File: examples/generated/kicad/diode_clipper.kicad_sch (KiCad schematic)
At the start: 3 parts

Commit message: Attempt to fix more terminal issues.
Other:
- moved on the sheet: D1
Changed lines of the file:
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@@
+    )
+  )
+  (symbol (lib_id "GND") (at 56.00 105.62 0) (unit 1)
+    (in_bom yes) (on_board yes)
+    (property "Reference" "#PWR0001" (at 56.0 101.81 0)
+      (effects (font (size 1.27 1.27)) hide)
+    )
+    (property "Value" "GND" (at 56.0 109.43 0)
+      (effects (font (size 1.27 1.27)))
+    )
+    (property "Footprint" "" (at 0 0 0)
+      (effects (font (size 1.27 1.27)) hide)
+    )
+    (property "Datasheet" "" (at 0 0 0)
+      (effects (font (size 1.27 1.27)) hide)
     )
   )
@@
     )
   )
-  (symbol (lib_id "DIODE") (at 90.00 112.00 0) (unit 1)
+  (symbol (lib_id "DIODE") (at 96.35 95.08 270) (unit 1)
     (in_bom yes) (on_board yes)
-    (property "Reference" "D1" (at 90.0 104.0 0)
+    (property "Reference" "D1" (at 96.35 87.08 0)
       (effects (font (size 1.27 1.27)))
     )
-    (property "Value" "D4148" (at 90.0 120.0 0)
+    (property "Value" "D4148" (at 96.35 103.08 0)
       (effects (font (size 1.27 1.27)))
     )
@@
     )
   )
-  (symbol (lib_id "GND") (at 56.00 105.62 0) (unit 1)
+  (symbol (lib_id "GND") (at 96.35 112.16 0) (unit 1)
     (in_bom yes) (on_board yes)
-    (property "Reference" "#PWR0001" (at 56.0 101.81 0)
+    (property "Reference" "#PWR0002" (at 96.35 108.35 0)
       (effects (font (size 1.27 1.27)) hide)
     )
-    (property "Value" "GND" (at 56.0 109.43 0)
+    (property "Value" "GND" (at 96.35 115.97 0)
       (effects (font (size 1.27 1.27)))
     )
@@
     )
   )
-  (symbol (lib_id "GND") (at 105.08 118.00 0) (unit 1)
-    (in_bom yes) (on_board yes)
-    (property "Reference" "#PWR0002" (at 105.08 114.19 0)
-      (effects (font (size 1.27 1.27)) hide)
-    )
-    (property "Value" "GND" (at 105.08 121.81 0)
-      (effects (font (size 1.27 1.27)))
-    )
-    (property "Footprint" "" (at 0 0 0)
-      (effects (font (size 1.27 1.27)) hide)
-    )
-    (property "Datasheet" "" (at 0 0 0)
-      (effects (font (size 1.27 1.27)) hide)
-    )
+  (wire (pts (xy 96.35 100.16) (xy 96.35 112.16))
+    (stroke (width 0) (type solid) (color 0 0 0 0))
   )
   (wire (pts (xy 56.00 93.62) (xy 56.00 105.62))
-    (stroke (width 0) (type solid) (color 0 0 0 0))
-  )
-  (wire (pts (xy 95.08 112.00) (xy 105.08 112.00))
-    (stroke (width 0) (type solid) (color 0 0 0 0))
-  )
-  (wire (pts (xy 105.08 112.00) (xy 105.08 118.00))
     (stroke (width 0) (type solid) (color 0 0 0 0))
   )
@@
     (stroke (width 0) (type solid) (color 0 0 0 0))
   )
-  (wire (pts (xy 96.35 78.00) (xy 98.50 78.00))
-    (stroke (width 0) (type solid) (color 0 0 0 0))
-  )
-  (wire (pts (xy 98.50 78.00) (xy 98.50 105.00))
-    (stroke (width 0) (type solid) (color 0 0 0 0))
-  )
-  (wire (pts (xy 98.50 105.00) (xy 82.50 105.00))
-    (stroke (width 0) (type solid) (color 0 0 0 0))
-  )
-  (wire (pts (xy 82.50 105.00) (xy 82.50 112.00))
-    (stroke (width 0) (type solid) (color 0 0 0 0))
-  )
-  (wire (pts (xy 82.50 112.00) (xy 84.92 112.00))
+  (wire (pts (xy 96.35 78.00) (xy 96.35 90.00))
     (stroke (width 0) (type solid) (color 0 0 0 0))
   )
@@
   (symbol_instances
     (path "/2c9e1e1c-69f0-5312-966c-7e56fb048925" (reference "V1") (unit 1) (value "SIN(0 5 1k)") (footprint ""))
+    (path "/229331e1-49b2-5d63-84c6-e3f127e9d83d" (reference "#PWR0001") (unit 1) (value "GND") (footprint ""))
     (path "/2c8aff2b-0935-51d8-b11f-1b19ccafeed0" (reference "R1") (unit 1) (value "1k") (footprint ""))
     (path "/6d337348-46f7-501d-8787-9fc457eabff9" (reference "D1") (unit 1) (value "D4148") (footprint ""))
-    (path "/229331e1-49b2-5d63-84c6-e3f127e9d83d" (reference "#PWR0001") (unit 1) (value "GND") (footprint ""))
     (path "/331ec4ee-80da-5867-9867-b03498e7d5de" (reference "#PWR0002") (unit 1) (value "GND") (footprint ""))
   )

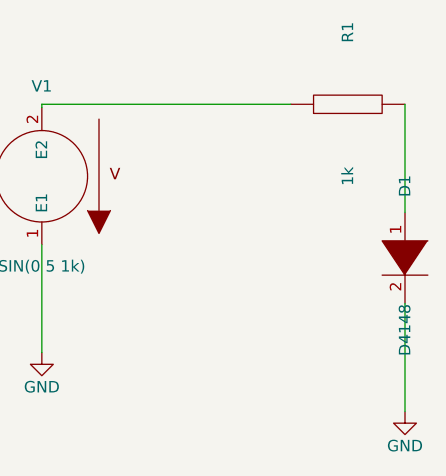
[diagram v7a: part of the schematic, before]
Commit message: Attempt again to fix up Common Emitter
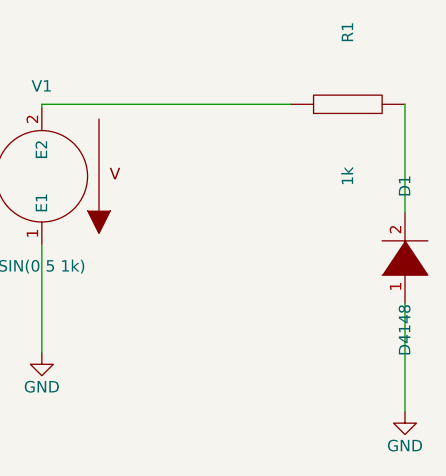
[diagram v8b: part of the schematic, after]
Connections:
- net GND: now also D1.1 (K); no longer D1.2 (A)
- net at R1.2: now also D1.2 (A); no longer D1.1 (K)
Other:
- moved on the sheet: D1
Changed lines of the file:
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@@
     )
   )
-  (symbol (lib_id "DIODE") (at 96.35 95.08 270) (unit 1)
+  (symbol (lib_id "DIODE") (at 96.35 95.08 90) (unit 1)
     (in_bom yes) (on_board yes)
     (property "Reference" "D1" (at 96.35 87.08 0)
